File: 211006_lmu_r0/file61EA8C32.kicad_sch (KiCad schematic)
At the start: 15 parts, among them U8 ADuM7641A

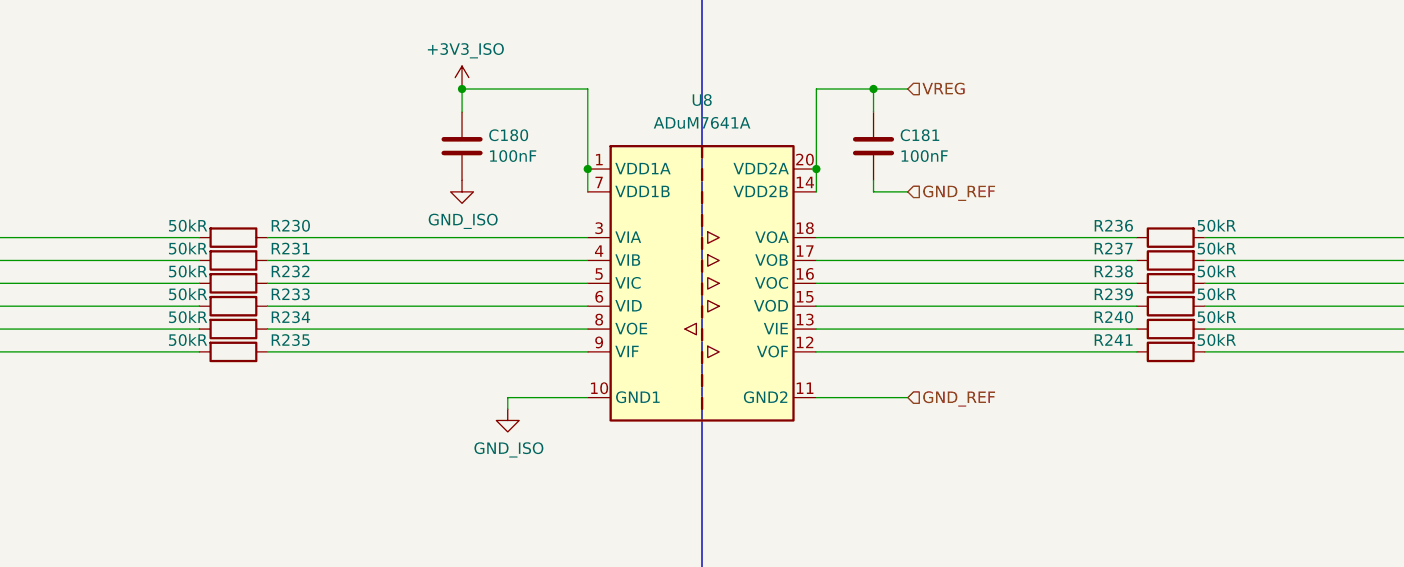
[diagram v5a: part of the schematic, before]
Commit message: silkscreen changes, shifting bun leds
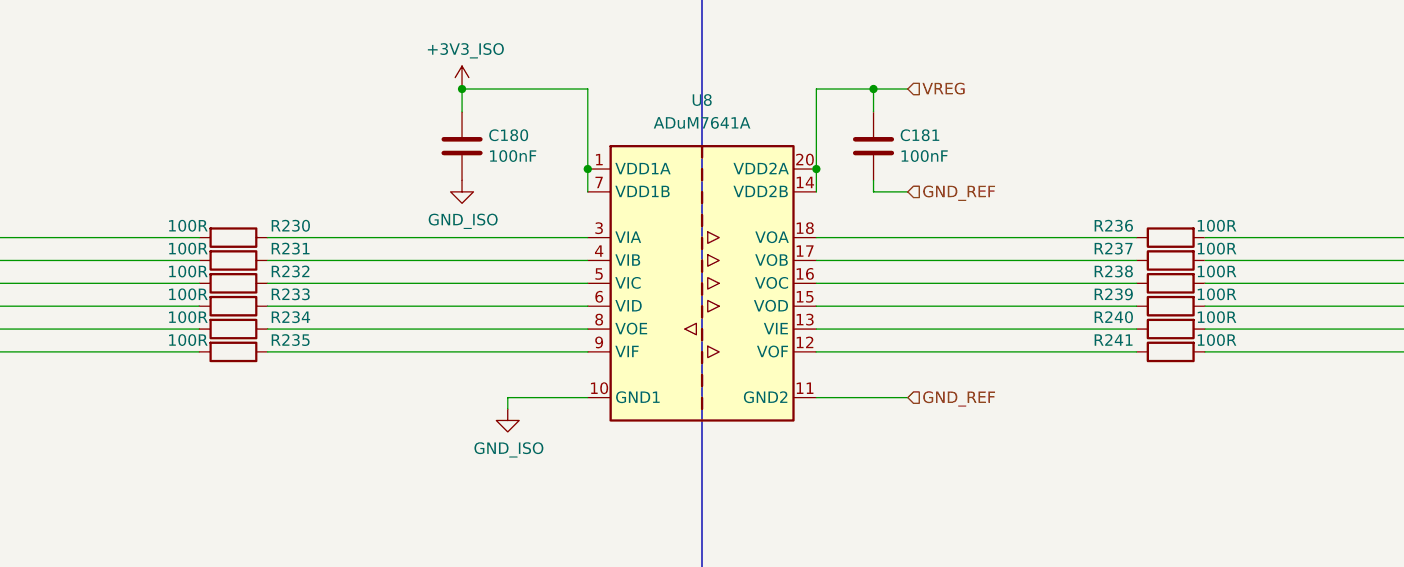
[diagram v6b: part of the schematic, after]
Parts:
- R230, R231, R232, R233, R234, R235, R236, R237, R238, R239, R240, R241: value 50kR -> 100R
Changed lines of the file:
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@@
     (in_bom yes) (on_board yes)
     (property "Reference" "R233" (id 0) (at 99.06 100.33 90))
-    (property "Value" "50kR" (id 1) (at 87.63 100.33 90))
+    (property "Value" "100R" (id 1) (at 87.63 100.33 90))
     (property "Footprint" "Resistor_SMD:R_0603_1608Metric_Pad0.98x0.95mm_HandSolder" (id 2) (at 92.71 99.822 90)
       (effects (font (size 1.27 1.27)) hide)
@@
     (in_bom yes) (on_board yes)
     (property "Reference" "R230" (id 0) (at 99.06 92.71 90))
-    (property "Value" "50kR" (id 1) (at 87.63 92.71 90))
+    (property "Value" "100R" (id 1) (at 87.63 92.71 90))
     (property "Footprint" "Resistor_SMD:R_0603_1608Metric_Pad0.98x0.95mm_HandSolder" (id 2) (at 92.71 92.202 90)
       (effects (font (size 1.27 1.27)) hide)
@@
     (in_bom yes) (on_board yes)
     (property "Reference" "R238" (id 0) (at 190.5 97.79 90))
-    (property "Value" "50kR" (id 1) (at 201.93 97.79 90))
+    (property "Value" "100R" (id 1) (at 201.93 97.79 90))
     (property "Footprint" "Resistor_SMD:R_0603_1608Metric_Pad0.98x0.95mm_HandSolder" (id 2) (at 196.85 97.282 90)
       (effects (font (size 1.27 1.27)) hide)
@@
     (in_bom yes) (on_board yes)
     (property "Reference" "R232" (id 0) (at 99.06 97.79 90))
-    (property "Value" "50kR" (id 1) (at 87.63 97.79 90))
+    (property "Value" "100R" (id 1) (at 87.63 97.79 90))
     (property "Footprint" "Resistor_SMD:R_0603_1608Metric_Pad0.98x0.95mm_HandSolder" (id 2) (at 92.71 97.282 90)
       (effects (font (size 1.27 1.27)) hide)
@@
     (in_bom yes) (on_board yes)
     (property "Reference" "R235" (id 0) (at 99.06 105.41 90))
-    (property "Value" "50kR" (id 1) (at 87.63 105.41 90))
+    (property "Value" "100R" (id 1) (at 87.63 105.41 90))
     (property "Footprint" "Resistor_SMD:R_0603_1608Metric_Pad0.98x0.95mm_HandSolder" (id 2) (at 92.71 104.902 90)
       (effects (font (size 1.27 1.27)) hide)
@@
     (in_bom yes) (on_board yes)
     (property "Reference" "R231" (id 0) (at 99.06 95.25 90))
-    (property "Value" "50kR" (id 1) (at 87.63 95.25 90))
+    (property "Value" "100R" (id 1) (at 87.63 95.25 90))
     (property "Footprint" "Resistor_SMD:R_0603_1608Metric_Pad0.98x0.95mm_HandSolder" (id 2) (at 92.71 94.742 90)
       (effects (font (size 1.27 1.27)) hide)
@@
     (in_bom yes) (on_board yes)
     (property "Reference" "R236" (id 0) (at 190.5 92.71 90))
-    (property "Value" "50kR" (id 1) (at 201.93 92.71 90))
+    (property "Value" "100R" (id 1) (at 201.93 92.71 90))
     (property "Footprint" "Resistor_SMD:R_0603_1608Metric_Pad0.98x0.95mm_HandSolder" (id 2) (at 196.85 92.202 90)
       (effects (font (size 1.27 1.27)) hide)
@@
     (in_bom yes) (on_board yes)
     (property "Reference" "R239" (id 0) (at 190.5 100.33 90))
-    (property "Value" "50kR" (id 1) (at 201.93 100.33 90))
+    (property "Value" "100R" (id 1) (at 201.93 100.33 90))
     (property "Footprint" "Resistor_SMD:R_0603_1608Metric_Pad0.98x0.95mm_HandSolder" (id 2) (at 196.85 99.822 90)
       (effects (font (size 1.27 1.27)) hide)
@@
     (in_bom yes) (on_board yes)
     (property "Reference" "R234" (id 0) (at 99.06 102.87 90))
-    (property "Value" "50kR" (id 1) (at 87.63 102.87 90))
+    (property "Value" "100R" (id 1) (at 87.63 102.87 90))
     (property "Footprint" "Resistor_SMD:R_0603_1608Metric_Pad0.98x0.95mm_HandSolder" (id 2) (at 92.71 102.362 90)
       (effects (font (size 1.27 1.27)) hide)
@@
     (in_bom yes) (on_board yes)
     (property "Reference" "R237" (id 0) (at 190.5 95.25 90))
-    (property "Value" "50kR" (id 1) (at 201.93 95.25 90))
+    (property "Value" "100R" (id 1) (at 201.93 95.25 90))
     (property "Footprint" "Resistor_SMD:R_0603_1608Metric_Pad0.98x0.95mm_HandSolder" (id 2) (at 196.85 94.742 90)
       (effects (font (size 1.27 1.27)) hide)
@@
     (in_bom yes) (on_board yes)
     (property "Reference" "R240" (id 0) (at 190.5 102.87 90))
-    (property "Value" "50kR" (id 1) (at 201.93 102.87 90))
+    (property "Value" "100R" (id 1) (at 201.93 102.87 90))
     (property "Footprint" "Resistor_SMD:R_0603_1608Metric_Pad0.98x0.95mm_HandSolder" (id 2) (at 196.85 102.362 90)
       (effects (font (size 1.27 1.27)) hide)
@@
     (in_bom yes) (on_board yes)
     (property "Reference" "R241" (id 0) (at 190.5 105.41 90))
-    (property "Value" "50kR" (id 1) (at 201.93 105.41 90))
+    (property "Value" "100R" (id 1) (at 201.93 105.41 90))
     (property "Footprint" "Resistor_SMD:R_0603_1608Metric_Pad0.98x0.95mm_HandSolder" (id 2) (at 196.85 104.902 90)
       (effects (font (size 1.27 1.27)) hide)

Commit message: started to export and fix things
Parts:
- U8: Manufacturer (none) -> -
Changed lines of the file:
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@@
+      (effects (font (size 1.27 1.27)) hide)
+    )
+    (property "Manufacturer" "-" (id 4) (at 144.78 99.06 0)
       (effects (font (size 1.27 1.27)) hide)
     )
